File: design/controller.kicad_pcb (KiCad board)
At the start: 2 copper layers, 23 parts, among them U1 ProMicro

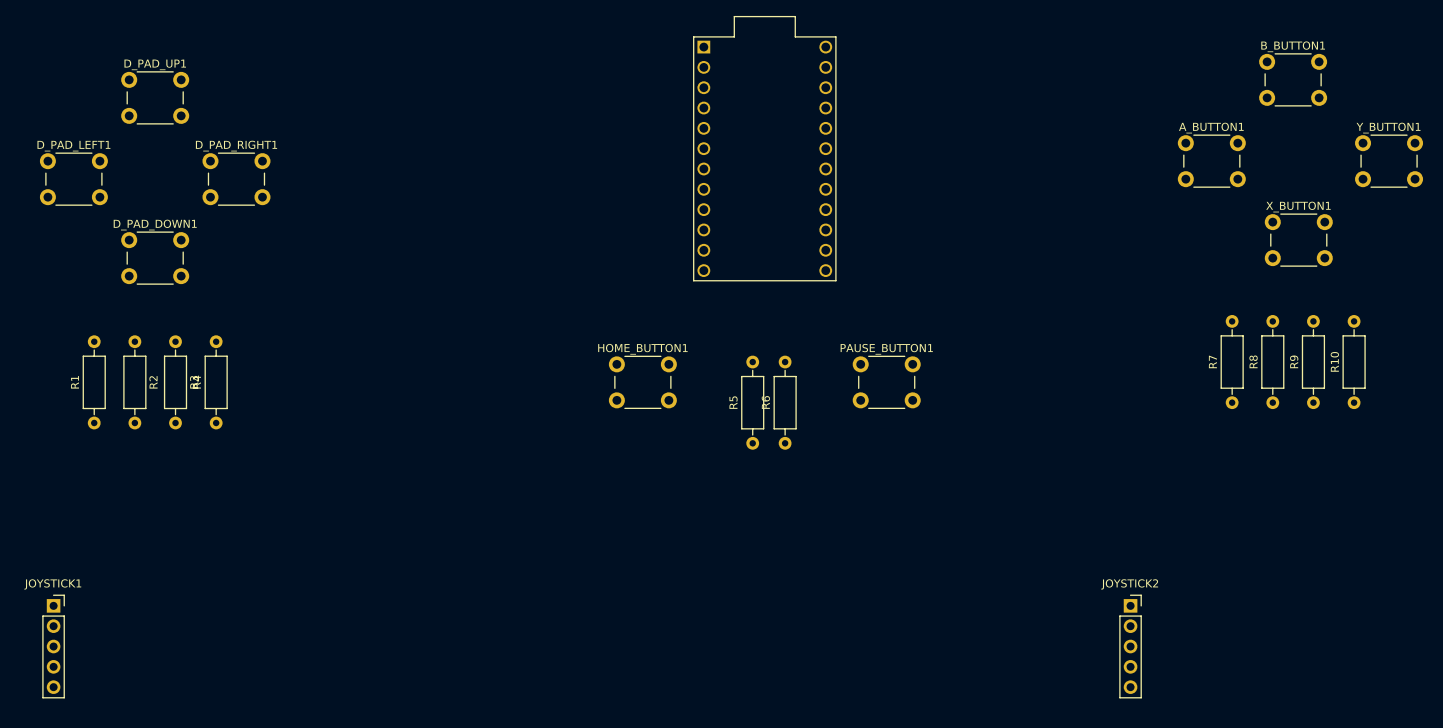
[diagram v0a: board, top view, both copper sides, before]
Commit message: Fixing controller design documents
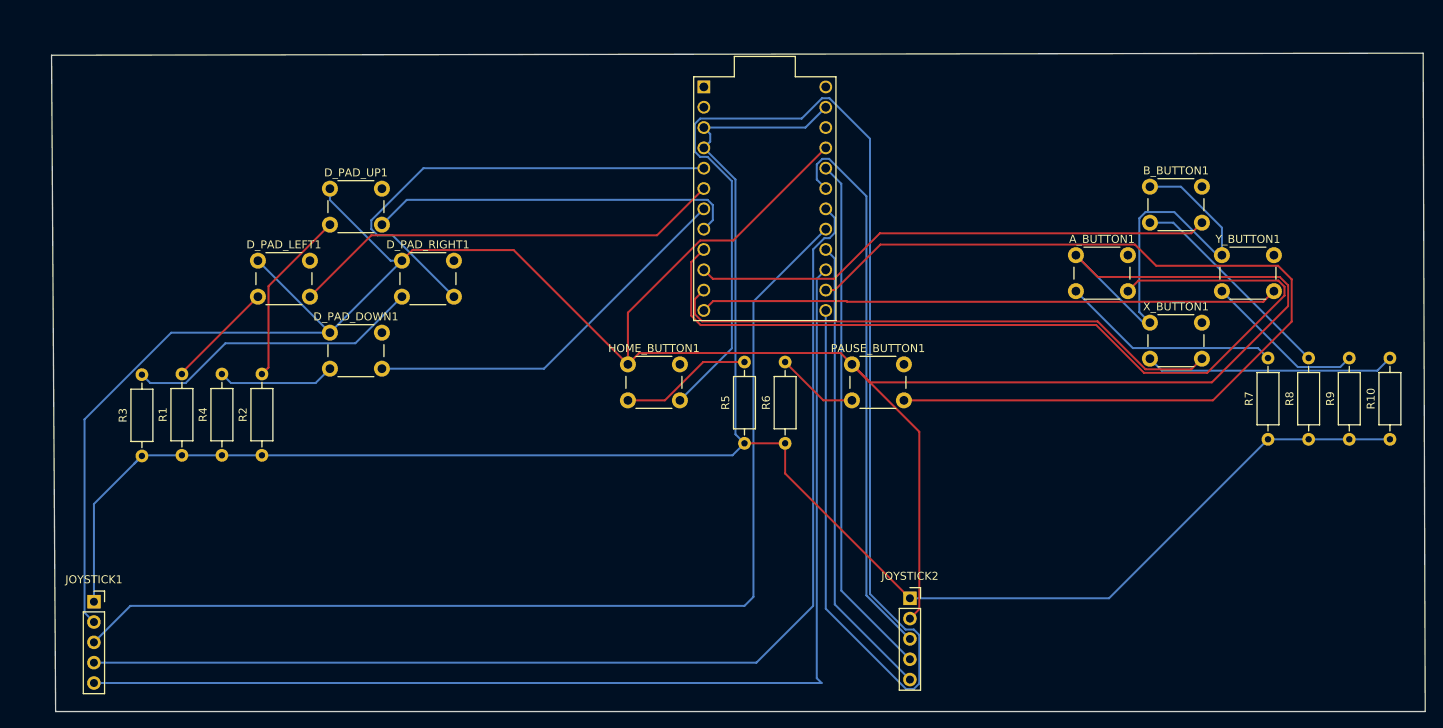
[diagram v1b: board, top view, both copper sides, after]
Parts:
- A_BUTTON1, B_BUTTON1, D_PAD_DOWN1, D_PAD_LEFT1, D_PAD_RIGHT1, D_PAD_UP1, HOME_BUTTON1, PAUSE_BUTTON1, X_BUTTON1, Y_BUTTON1: value SW_Push -> 1825910-6; footprint Button_Switch_THT:SW_PUSH_6mm_H5mm -> controller:SW_PUSH_4_PIN
- moved D_PAD_LEFT1 29.0 mm to (86.5, 45.8)
- moved D_PAD_UP1 28.5 mm to (95.5, 36.8)
- moved D_PAD_DOWN1 27.6 mm to (95.5, 54.8)
- moved JOYSTICK2 27.6 mm to (168.0, 88.0)
- moved D_PAD_RIGHT1 27.0 mm to (104.5, 45.8)
- moved Y_BUTTON1 22.5 mm to (207.0, 45.1)
- moved B_BUTTON1 21.4 mm to (198.0, 36.5)
- moved R2 21.3 mm to (87.0, 70.1), turned to 90 degrees
- moved X_BUTTON1 19.8 mm to (198.0, 53.5)
- moved A_BUTTON1 19.6 mm to (188.8, 45.1)
- moved R3 14.9 mm to (72.0, 70.2), turned to 90 degrees
- moved R1 11.7 mm to (77.0, 70.1)
- moved R10 6.41 mm to (228.0, 68.1)
- moved R7 6.41 mm to (212.8, 68.1)
- moved R8 6.41 mm to (217.8, 68.1)
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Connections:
- A_BUTTON1 pad 1: Net-(A_BUTTON1-Pad1) -> VCC
- A_BUTTON1 pad 2: /VCC+ -> Net-(A_BUTTON1-Pad2)
- B_BUTTON1 pad 1: Net-(B_BUTTON1-Pad1) -> VCC
- B_BUTTON1 pad 2: /VCC+ -> Net-(B_BUTTON1-Pad2)
- D_PAD_DOWN1 pad 1: Net-(D_PAD_DOWN1-Pad1) -> VCC
- D_PAD_DOWN1 pad 2: /VCC+ -> Net-(D_PAD_DOWN1-Pad2)
- D_PAD_LEFT1 pad 1: Net-(D_PAD_LEFT1-Pad1) -> VCC
- D_PAD_LEFT1 pad 2: /VCC+ -> Net-(D_PAD_LEFT1-Pad2)
- D_PAD_RIGHT1 pad 1: Net-(D_PAD_RIGHT1-Pad1) -> VCC
- D_PAD_RIGHT1 pad 2: /VCC+ -> Net-(D_PAD_RIGHT1-Pad2)
- D_PAD_UP1 pad 1: Net-(D_PAD_UP1-Pad1) -> VCC
- D_PAD_UP1 pad 2: /VCC+ -> Net-(D_PAD_UP1-Pad2)
- HOME_BUTTON1 pad 1: Net-(HOME_BUTTON1-Pad1) -> VCC
- HOME_BUTTON1 pad 2: /VCC+ -> Net-(HOME_BUTTON1-Pad2)
- JOYSTICK1 pad 2: /PIN_A1 -> VCC
- JOYSTICK1 pad 3: /VCC+ -> /PIN_A0
- JOYSTICK1 pad 4: /PIN_14 -> /PIN_A1
- JOYSTICK1 pad 5: /PIN_A0 -> /PIN_14
- JOYSTICK2 pad 2: /PIN_A3 -> VCC
- JOYSTICK2 pad 3: /VCC+ -> /PIN_A2
- JOYSTICK2 pad 4: /PIN_15 -> /PIN_A3
- JOYSTICK2 pad 5: /PIN_A2 -> /PIN_15
- PAUSE_BUTTON1 pad 1: Net-(PAUSE_BUTTON1-Pad1) -> VCC
- PAUSE_BUTTON1 pad 2: /VCC+ -> Net-(PAUSE_BUTTON1-Pad2)
- R1 pad 2: Net-(D_PAD_LEFT1-Pad1) -> Net-(D_PAD_LEFT1-Pad2)
- R2 pad 2: Net-(D_PAD_DOWN1-Pad1) -> Net-(D_PAD_UP1-Pad2)
- R3 pad 2: Net-(D_PAD_UP1-Pad1) -> Net-(D_PAD_RIGHT1-Pad2)
- R4 pad 2: Net-(D_PAD_RIGHT1-Pad1) -> Net-(D_PAD_DOWN1-Pad2)
- R5 pad 2: Net-(HOME_BUTTON1-Pad1) -> Net-(HOME_BUTTON1-Pad2)
- R6 pad 2: Net-(PAUSE_BUTTON1-Pad1) -> Net-(PAUSE_BUTTON1-Pad2)
- R7 pad 2: Net-(A_BUTTON1-Pad1) -> Net-(A_BUTTON1-Pad2)
- R8 pad 2: Net-(R8-Pad2) -> Net-(B_BUTTON1-Pad2)
- R9 pad 2: Net-(B_BUTTON1-Pad1) -> Net-(R9-Pad2)
- U1 pad 21: /VCC+ -> VCC
- X_BUTTON1 pad 1: Net-(R8-Pad2) -> VCC
- X_BUTTON1 pad 2: /VCC+ -> Net-(R10-Pad2)
- Y_BUTTON1 pad 1: Net-(R10-Pad2) -> VCC
- Y_BUTTON1 pad 2: /VCC+ -> Net-(R9-Pad2)
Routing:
- net VCC: track 0.00 -> 383.2 mm
- net GND: track 0.00 -> 255.7 mm
- net /PIN_10: track 0.00 -> 189.7 mm
- net /PIN_A1: track 0.00 -> 144.4 mm
- net /PIN_14: track 0.00 -> 143.3 mm
- net /PIN_A0: track 0.00 -> 134.5 mm
- net /PIN_16: track 0.00 -> 120.2 mm
- net /PIN_6: track 0.00 -> 111.6 mm
- net /PIN_9: track 0.00 -> 72.3 mm
- net /PIN_8: track 0.00 -> 70.3 mm
- net /PIN_A2: track 0.00 -> 69.5 mm
- net /PIN_A3: track 0.00 -> 65.7 mm
- net /PIN_7: track 0.00 -> 65.6 mm
- net /PIN_2: track 0.00 -> 59.2 mm
- net /PIN_15: track 0.00 -> 58.1 mm
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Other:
- board outline added: 171.7 x 82.3 mm

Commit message: Updating Desgin Files
Adding in Gerber files, removing unnecessary files
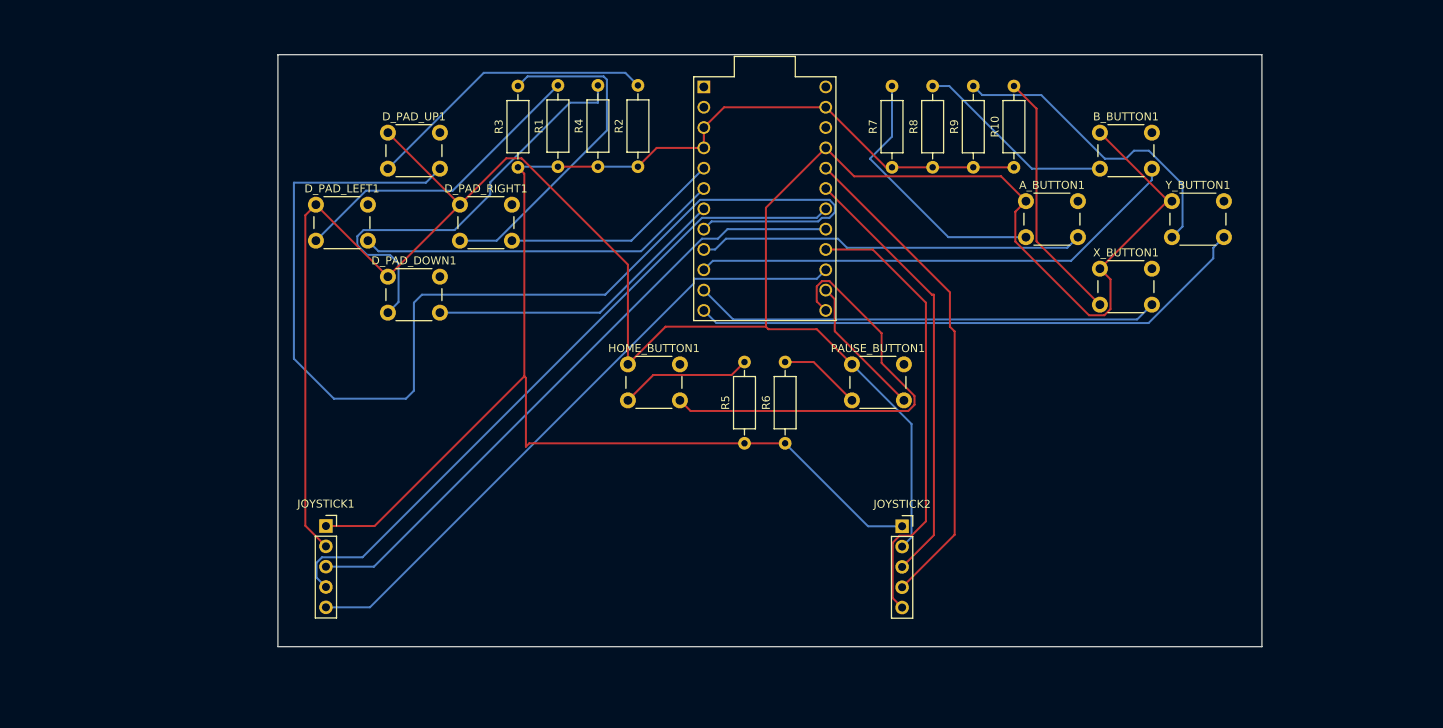
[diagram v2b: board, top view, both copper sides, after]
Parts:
- moved R1 59.3 mm to (124.0, 34.0)
- moved R2 59.3 mm to (134.0, 34.0)
- moved R3 59.3 mm to (119.0, 34.1)
- moved R4 59.3 mm to (129.0, 34.0)
- moved R10 58.0 mm to (181.0, 34.1)
- moved R7 58.0 mm to (165.8, 34.1)
- moved R8 58.0 mm to (170.8, 34.1)
- moved R9 58.0 mm to (175.9, 34.1)
- moved JOYSTICK1 30.5 mm to (95.0, 78.9)
- moved D_PAD_DOWN1 10.1 mm to (102.8, 47.8)
- moved D_PAD_LEFT1 10.1 mm to (93.8, 38.8)
- moved D_PAD_RIGHT1 10.1 mm to (111.8, 38.8)
- moved D_PAD_UP1 10.1 mm to (102.8, 29.8)
- moved A_BUTTON1 9.20 mm to (182.5, 38.3)
- moved B_BUTTON1 9.20 mm to (191.8, 29.8)
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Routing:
- net /PIN_10: track 189.7 -> 55.4 mm
- net /PIN_16: track 120.2 -> 17.8 mm
- net /PIN_5: track 46.4 -> 145.8 mm
- net VCC: track 383.2 -> 287.6 mm
- net GND: track 255.7 -> 189.1 mm
- net /PIN_6: track 111.6 -> 48.3 mm
- net /PIN_14: track 143.3 -> 80.3 mm
- net /PIN_A1: track 144.4 -> 85.5 mm
- net /PIN_A0: track 134.5 -> 80.0 mm
- net Net-(D_PAD_DOWN1-Pad2): track 14.7 -> 54.0 mm
- net /PIN_2: track 59.2 -> 27.7 mm
- net Net-(D_PAD_LEFT1-Pad2): track 13.6 -> 38.3 mm
- net Net-(R9-Pad2): track 20.3 -> 39.2 mm
- net /PIN_A2: track 69.5 -> 54.7 mm
- net Net-(D_PAD_UP1-Pad2): track 22.2 -> 36.9 mm
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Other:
- board size 171.7 x 82.3 mm -> 123 x 74 mm
